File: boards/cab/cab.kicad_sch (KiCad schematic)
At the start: 39 parts, among them J1 Conn_01x08_Female, J2 Conn_01x08_Female, J3 Conn_01x08_Female, J4 Conn_01x08_Female, Q1 SI2308A, Q2 S8550, Q3 BC817-40,215, Q4 S8550, Q5 BC817-40,215, Q6 S8550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

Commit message: Created PCB
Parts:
- added R10: 50k, Resistor_SMD:R_0805_2012Metric, symbol Device:R
- added R11: 4.7k, Resistor_SMD:R_0805_2012Metric, symbol Device:R
- added SW1: SW_Push, Connector_PinHeader_2.54mm:PinHeader_1x02_P2.54mm_Vertical, symbol Switch:SW_Push
- L3: footprint StackCabinet:Solenoid -> TerminalBlock_4Ucon:TerminalBlock_4Ucon_1x02_P3.50mm_Vertical; LCSC. Part# (none) -> C474892; Mfr. Part# (none) -> KF350-3.5-2P
- Q2, Q3, Q4, Q5, Q6, Q7, Q8: footprint Package_TO_SOT_THT:TO-220-3_Vertical -> Package_TO_SOT_SMD:SOT-23
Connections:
- net 5V: now also R10.2
- net GND: now also SW1.1; no longer U1.4 (ON/OFF)
- net CAB_STATE: now reaches U3.10 (PB4)
- net CAB_STATE: now also R10.1, SW1.2
- net RxD: now reaches U3.11 (PB3)
- net TxD: now reaches U3.12 (PB2)
- net 24V_EN: now reaches U3.13 (PB1)
- net 24V_EN: now also U1.4 (ON/OFF)
- net at U3.19 (~{RESET}/PA0): now also R11.1
- new net UPDI: R11.2
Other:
- moved on the sheet: C8, C9

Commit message: Finished schematic
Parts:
- added C10: 0.1uF, Capacitor_SMD:C_0805_2012Metric, symbol Device:C
- added R12: 1k, Resistor_SMD:R_0805_2012Metric, symbol Device:R
- C1, C2: footprint Capacitor_THT:C_Radial_D10.0mm_H16.0mm_P5.00mm -> Capacitor_THT:C_Radial_D12.5mm_H20.0mm_P5.00mm; LCSC Part# C397095 -> (none); LCSC. Part# (none) -> C269945; Mfr. Part# ECR1VGK471MFA100016 -> OGPL41H471MF
- C3, C4, C8, C9: LCSC Part# C91185 -> (none); LCSC. Part# (none) -> C91185
- C5: LCSC Part# C221302 -> (none); LCSC. Part# (none) -> C221302
- C6: LCSC Part# C442870 -> (none); LCSC. Part# (none) -> C442870
- C7: LCSC Part# C152864 -> (none); LCSC. Part# (none) -> C152864
- D1, D2, D3: LCSC Part# C3015221 -> (none); LCSC. Part# (none) -> C3015221
- J1, J2, J3, J4: LCSC. Part# (none) -> C691120; Mfr. Part# (none) -> C691120
- L1: LCSC part# C5142143 -> (none); LCSC. Part# (none) -> C5142143
- L2: footprint Inductor_SMD:L_Wuerth_WE-DD-Typ-L-Typ-XL-Typ-XXL -> Inductor_SMD:L_6.3x6.3_H3; LCSC part# C2846222 -> (none); LCSC. Part# (none) -> C5189964; Mfr. Part# ACPR1208S680MT -> CYA0650-68UH
- Q1: LCSC Part# C347491 -> (none); LCSC. Part# (none) -> C347491
- Q2, Q4, Q6, Q8: LCSC Part# C181159 -> (none); LCSC. Part# (none) -> C181159
- Q3, Q5, Q7: LCSC Part# C52801 -> (none); LCSC. Part# (none) -> C52801
- R1: renamed from R2; LCSC Part# C218493 -> (none); LCSC. Part# (none) -> C218493
- R10: LCSC Part# C2828840 -> (none); LCSC. Part# (none) -> C2828840
- R11: LCSC Part# C115310 -> (none); LCSC. Part# (none) -> C115310
- R2: renamed from R1; LCSC Part# C2828840 -> (none); LCSC. Part# (none) -> C2828840
- R3, R4, R5, R6, R7, R8, R9: LCSC Part# C2902822 -> (none); LCSC. Part# (none) -> C412430; Mfr Part# AR05CTC1000 -> (none); Mfr. Part# (none) -> SWR05JTEV1001
- SW1: LCSC. Part# C393938 -> C397293; Mfr. Part# TS665CJ -> B3F-1005
- U1: footprint Package_SO:SOIC-8_3.9x4.9mm_P1.27mm -> Package_SO:SOP-8_3.9x4.9mm_P1.27mm
- U2: footprint Package_SO:SOIC-8_3.9x4.9mm_P1.27mm -> Package_SO:SOP-8_3.9x4.9mm_P1.27mm; LCSC Part# C61063 -> (none); LCSC. Part# (none) -> C61063
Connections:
- net 24V: now also D2.1 (K); no longer D3.1 (K)
- net 5V: now also C10.1
- net B_PWM: now also R9.1; no longer R5.1
- net GND: now also D3.2 (A), C10.2; no longer D2.2 (A)
- net G_PWM: now also R7.1; no longer R4.1
- net LED1_PWM: now also R5.1; no longer R7.1
- net LED3_PWM: now also R12.1; no longer R9.1
- net R_PWM: now also R4.1; no longer R3.1
- net SOL_EN: now also R3.1; no longer Q1.1 (G)
- net at R7.2: now also Q5.1 (B); no longer Q4.1 (B)
- net at Q8.1 (B): now also R12.2; no longer R9.2
- net at Q7.1 (B): now also R9.2; no longer R5.2
- net at L3.2, Q1.3 (D): now also D2.2 (A); no longer D3.2 (A)
- net at Q3.1 (B): now also R4.2; no longer R3.2
- net at L2.1, U2.2 (OUT): now also D3.1 (K); no longer D2.1 (K)
- new net: Q1.1 (G), R3.2
- new net: Q4.1 (B), R5.2
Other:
- moved on the sheet: SW1

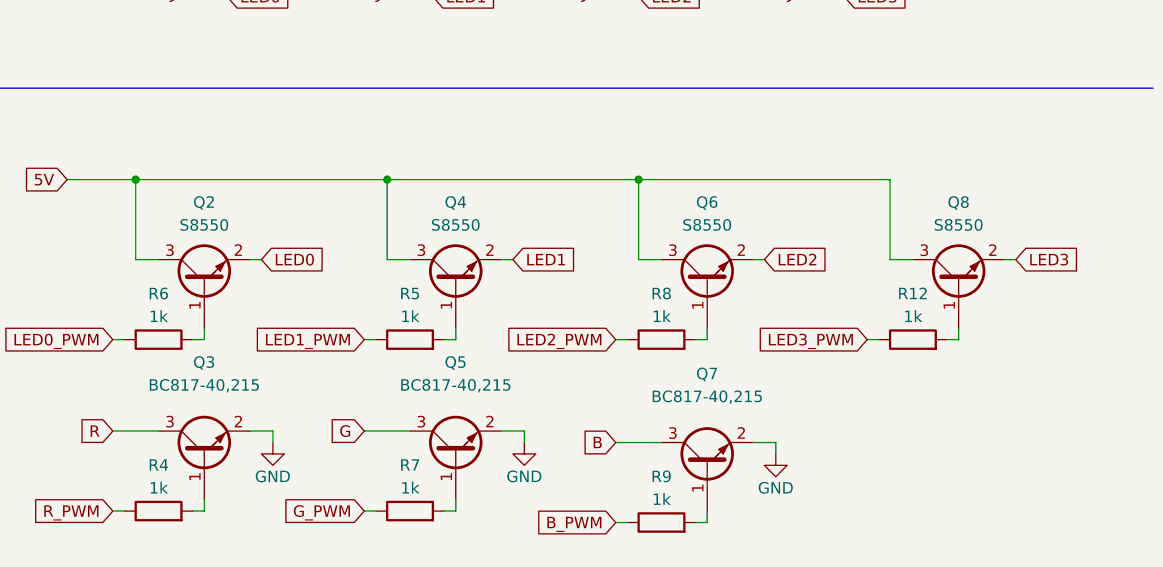
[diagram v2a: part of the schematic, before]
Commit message: Fixed mosfet footprint
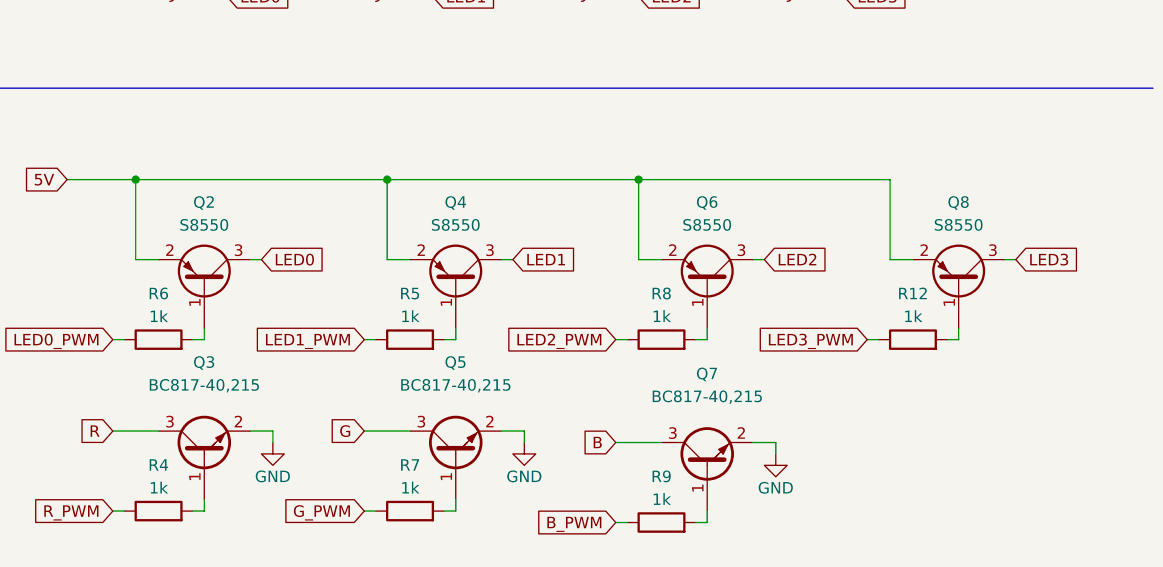
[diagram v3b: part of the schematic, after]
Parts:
- removed Q4, Q6, Q8: S8550, Package_TO_SOT_SMD:SOT-23, symbol Transistor_BJT:2SC1945
- added Q4, Q6, Q8: S8550, Package_TO_SOT_SMD:SOT-23, symbol Transistor_BJT:BC807
- Q2: symbol Transistor_BJT:2SC1945 -> Transistor_BJT:BC807
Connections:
- net 5V: now also Q2.2 (E), Q4.2 (E), Q6.2 (E), Q8.2 (E); no longer Q2.3 (C)
- net LED0: now also Q2.3 (C); no longer Q2.2 (E)
- net LED1: now also Q4.3 (C)
- net LED2: now also Q6.3 (C)
- net LED3: now also Q8.3 (C)
- net at R12.2: now also Q8.1 (B)
- net at R5.2: now also Q4.1 (B)
- net at R8.2: now also Q6.1 (B)
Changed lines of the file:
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@@
     (pin "2")
-  )
-  (symbol (lib_id "Transistor_BJT:2SC1945") (at 262.89 74.93 90) (unit 1)
-    (in_bom yes) (on_board yes)
-    (property "Reference" "Q8" (id 0) (at 262.89 66.04 90))
-    (property "Value" "S8550" (id 1) (at 262.89 68.58 90))
-    (property "Footprint" "Package_TO_SOT_SMD:SOT-23" (id 2) (at 264.795 69.85 0)
-      (effects (font (size 1.27 1.27) italic) (justify left) hide)
-    )
-    (property "Datasheet" "https://datasheet.lcsc.com/lcsc/2205061000_Guangdong-Hottech-S8550_C181159.pdf" (id 3) (at 262.89 74.93 0)
-      (effects (font (size 1.27 1.27)) (justify left) hide)
-    )
-    (property "Mfr. Part#" "S8550" (id 4) (at 262.89 74.93 90)
-      (effects (font (size 1.27 1.27)) hide)
-    )
-    (property "LCSC Part#" "" (id 5) (at 262.89 74.93 90)
-      (effects (font (size 1.27 1.27)) hide)
-    )
-    (property "LCSC. Part#" "C181159" (id 6) (at 262.89 74.93 0)
-      (effects (font (size 1.27 1.27)) hide)
-    )
-    (pin "1")
-    (pin "2")
-    (pin "3")
   )
   (symbol (lib_id "Device:C") (at 123.19 41.91 0) (unit 1)
@@
     (pin "2")
   )
+  (symbol (lib_id "Transistor_BJT:BC807") (at 234.95 74.93 270) (mirror x) (unit 1)
+    (in_bom yes) (on_board yes)
+    (property "Reference" "Q6" (id 0) (at 234.95 66.04 90))
+    (property "Value" "S8550" (id 1) (at 234.95 68.58 90))
+    (property "Footprint" "Package_TO_SOT_SMD:SOT-23" (id 2) (at 233.045 69.85 0)
+      (effects (font (size 1.27 1.27) italic) (justify left) hide)
+    )
+    (property "Datasheet" "https://datasheet.lcsc.com/lcsc/2205061000_Guangdong-Hottech-S8550_C181159.pdf" (id 3) (at 234.95 74.93 0)
+      (effects (font (size 1.27 1.27)) (justify left) hide)
+    )
+    (property "Mfr. Part#" "S8550" (id 4) (at 234.95 74.93 90)
+      (effects (font (size 1.27 1.27)) hide)
+    )
+    (property "LCSC. Part#" "C181159" (id 6) (at 234.95 74.93 0)
+      (effects (font (size 1.27 1.27)) hide)
+    )
+    (pin "1")
+    (pin "2")
+    (pin "3")
+  )
   (symbol (lib_id "power:GND") (at 242.57 93.98 0) (unit 1)
     (in_bom yes) (on_board yes)
@@
     (pin "2")
   )
-  (symbol (lib_id "Transistor_BJT:2SC1945") (at 207.01 74.93 90) (unit 1)
-    (in_bom yes) (on_board yes)
-    (property "Reference" "Q4" (id 0) (at 207.01 66.04 90))
-    (property "Value" "S8550" (id 1) (at 207.01 68.58 90))
-    (property "Footprint" "Package_TO_SOT_SMD:SOT-23" (id 2) (at 208.915 69.85 0)
+  (symbol (lib_id "Transistor_BJT:BC807") (at 262.89 74.93 270) (mirror x) (unit 1)
+    (in_bom yes) (on_board yes)
+    (property "Reference" "Q8" (id 0) (at 262.89 66.04 90))
+    (property "Value" "S8550" (id 1) (at 262.89 68.58 90))
+    (property "Footprint" "Package_TO_SOT_SMD:SOT-23" (id 2) (at 260.985 69.85 0)
       (effects (font (size 1.27 1.27) italic) (justify left) hide)
     )
-    (property "Datasheet" "https://datasheet.lcsc.com/lcsc/2205061000_Guangdong-Hottech-S8550_C181159.pdf" (id 3) (at 207.01 74.93 0)
+    (property "Datasheet" "https://datasheet.lcsc.com/lcsc/2205061000_Guangdong-Hottech-S8550_C181159.pdf" (id 3) (at 262.89 74.93 0)
       (effects (font (size 1.27 1.27)) (justify left) hide)
     )
-    (property "Mfr. Part#" "S8550" (id 4) (at 207.01 74.93 90)
-      (effects (font (size 1.27 1.27)) hide)
-    )
-    (property "LCSC Part#" "" (id 5) (at 207.01 74.93 90)
-      (effects (font (size 1.27 1.27)) hide)
-    )
-    (property "LCSC. Part#" "C181159" (id 6) (at 207.01 74.93 0)
+    (property "Mfr. Part#" "S8550" (id 4) (at 262.89 74.93 90)
+      (effects (font (size 1.27 1.27)) hide)
+    )
+    (property "LCSC. Part#" "C181159" (id 6) (at 262.89 74.93 0)
       (effects (font (size 1.27 1.27)) hide)
     )
@@
     (pin "1")
   )
+  (symbol (lib_id "Transistor_BJT:BC807") (at 207.01 74.93 270) (mirror x) (unit 1)
+    (in_bom yes) (on_board yes)
+    (property "Reference" "Q4" (id 0) (at 207.01 66.04 90))
+    (property "Value" "S8550" (id 1) (at 207.01 68.58 90))
+    (property "Footprint" "Package_TO_SOT_SMD:SOT-23" (id 2) (at 205.105 69.85 0)
+      (effects (font (size 1.27 1.27) italic) (justify left) hide)
+    )
+    (property "Datasheet" "https://datasheet.lcsc.com/lcsc/2205061000_Guangdong-Hottech-S8550_C181159.pdf" (id 3) (at 207.01 74.93 0)
+      (effects (font (size 1.27 1.27)) (justify left) hide)
+    )
+    (property "Mfr. Part#" "S8550" (id 4) (at 207.01 74.93 90)
+      (effects (font (size 1.27 1.27)) hide)
+    )
+    (property "LCSC. Part#" "C181159" (id 6) (at 207.01 74.93 0)
+      (effects (font (size 1.27 1.27)) hide)
+    )
+    (pin "1")
+    (pin "2")
+    (pin "3")
+  )
   (symbol (lib_id "Device:C") (at 44.45 44.45 0) (unit 1)
     (in_bom yes) (on_board yes)
@@
     (pin "5")
   )
-  (symbol (lib_id "Transistor_BJT:2SC1945") (at 179.07 74.93 90) (unit 1)
+  (symbol (lib_id "Transistor_BJT:BC807") (at 179.07 74.93 270) (mirror x) (unit 1)
     (in_bom yes) (on_board yes)
     (property "Reference" "Q2" (id 0) (at 179.07 66.04 90))
     (property "Value" "S8550" (id 1) (at 179.07 68.58 90))
-    (property "Footprint" "Package_TO_SOT_SMD:SOT-23" (id 2) (at 180.975 69.85 0)
+    (property "Footprint" "Package_TO_SOT_SMD:SOT-23" (id 2) (at 177.165 69.85 0)
       (effects (font (size 1.27 1.27) italic) (justify left) hide)
     )
@@
     (pin "1")
   )
-  (symbol (lib_id "Transistor_BJT:2SC1945") (at 234.95 74.93 90) (unit 1)
-    (in_bom yes) (on_board yes)
-    (property "Reference" "Q6" (id 0) (at 234.95 66.04 90))
-    (property "Value" "S8550" (id 1) (at 234.95 68.58 90))
-    (property "Footprint" "Package_TO_SOT_SMD:SOT-23" (id 2) (at 236.855 69.85 0)
-      (effects (font (size 1.27 1.27) italic) (justify left) hide)
-    )
-    (property "Datasheet" "https://datasheet.lcsc.com/lcsc/2205061000_Guangdong-Hottech-S8550_C181159.pdf" (id 3) (at 234.95 74.93 0)
-      (effects (font (size 1.27 1.27)) (justify left) hide)
-    )
-    (property "Mfr. Part#" "S8550" (id 4) (at 234.95 74.93 90)
-      (effects (font (size 1.27 1.27)) hide)
-    )
-    (property "LCSC Part#" "" (id 5) (at 234.95 74.93 90)
-      (effects (font (size 1.27 1.27)) hide)
-    )
-    (property "LCSC. Part#" "C181159" (id 6) (at 234.95 74.93 0)
-      (effects (font (size 1.27 1.27)) hide)
-    )
-    (pin "1")
-    (pin "2")
-    (pin "3")
-  )
   (symbol (lib_id "power:GND") (at 191.77 29.21 0) (unit 1)
     (in_bom yes) (on_board yes)
@@
       (reference "Q3") (unit 1) (value "BC817-40,215") (footprint "Package_TO_SOT_SMD:SOT-23")
     )
-    (path "/59ddffe5-0dff-4bee-a16e-bf5bc8ab3f34"
+    (path "/773b2310-3334-4f95-9a81-1e66c9eb0eb2"
       (reference "Q4") (unit 1) (value "S8550") (footprint "Package_TO_SOT_SMD:SOT-23")
     )
@@
       (reference "Q5") (unit 1) (value "BC817-40,215") (footprint "Package_TO_SOT_SMD:SOT-23")
     )
-    (path "/fbeaaf82-15a7-47c8-9550-6b0c20c4284d"
+    (path "/21e6e123-f380-4d1f-aea4-53d262ccd85a"
       (reference "Q6") (unit 1) (value "S8550") (footprint "Package_TO_SOT_SMD:SOT-23")
     )
@@
       (reference "Q7") (unit 1) (value "BC817-40,215") (footprint "Package_TO_SOT_SMD:SOT-23")
     )
-    (path "/03c9e3a6-520e-43cf-ac75-75db95716ba5"
+    (path "/5d515d29-5c44-4bed-9ff1-10a60546f72b"
       (reference "Q8") (unit 1) (value "S8550") (footprint "Package_TO_SOT_SMD:SOT-23")
     )

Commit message: Placed Power, Attiny and LED power
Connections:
- net TxD is gone; now on net GDA: U3.12 (PB2)
- net 24V: now also C5.1, C7.1, L1.2, R2.2; no longer C6.1, L2.2, U2.3 (FB)
- net 24V_EN: now also U3.2 (PA3); no longer U3.13 (PB1)
- net 5V: now also C6.1, L2.2, U2.3 (FB); no longer C5.1, C7.1, L1.2, R2.2
- net G_PWM: now also U3.7 (PA6); no longer U3.2 (PA3)
- net LED1_PWM: now also U3.14 (PB0); no longer U3.6 (PA5)
- net LED2_PWM: now also U3.13 (PB1); no longer U3.7 (PA6)
- net R_PWM: now also U3.6 (PA5); no longer U3.1 (PA2)
- net SOL_EN: now also U3.1 (PA2); no longer U3.14 (PB0)
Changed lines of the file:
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@@
+    )
+  )
+  (global_label "R_PWM" (shape input) (at 137.16 143.51 0) (fields_autoplaced)
+    (effects (font (size 1.27 1.27)) (justify left))
+    (property "Intersheet References" "${INTERSHEET_REFS}" (id 0) (at 145.9836 143.5894 0)
+      (effects (font (size 1.27 1.27)) (justify left) hide)
     )
   )
@@
     )
   )
+  (global_label "LED1_PWM" (shape input) (at 137.16 153.67 0) (fields_autoplaced)
+    (effects (font (size 1.27 1.27)) (justify left))
+    (property "Intersheet References" "${INTERSHEET_REFS}" (id 0) (at 149.3702 153.7494 0)
+      (effects (font (size 1.27 1.27)) (justify left) hide)
+    )
+  )
   (global_label "LED3_PWM" (shape input) (at 252.73 81.28 180) (fields_autoplaced)
     (effects (font (size 1.27 1.27)) (justify right))
@@
     )
   )
-  (global_label "24V_EN" (shape input) (at 137.16 156.21 0) (fields_autoplaced)
-    (effects (font (size 1.27 1.27)) (justify left))
-    (property "Intersheet References" "${INTERSHEET_REFS}" (id 0) (at 146.5279 156.1306 0)
-      (effects (font (size 1.27 1.27)) (justify left) hide)
-    )
-  )
   (global_label "SOL_EN" (shape input) (at 45.72 158.75 180) (fields_autoplaced)
     (effects (font (size 1.27 1.27)) (justify right))
@@
     )
   )
-  (global_label "24V" (shape input) (at 115.57 81.28 0) (fields_autoplaced)
-    (effects (font (size 1.27 1.27)) (justify left))
-    (property "Intersheet References" "${INTERSHEET_REFS}" (id 0) (at 121.4907 81.2006 0)
+  (global_label "5V" (shape input) (at 115.57 81.28 0) (fields_autoplaced)
+    (effects (font (size 1.27 1.27)) (justify left))
+    (property "Intersheet References" "${INTERSHEET_REFS}" (id 0) (at 120.2812 81.2006 0)
       (effects (font (size 1.27 1.27)) (justify left) hide)
     )
@@
     )
   )
-  (global_label "LED2_PWM" (shape input) (at 137.16 146.05 0) (fields_autoplaced)
-    (effects (font (size 1.27 1.27)) (justify left))
-    (property "Intersheet References" "${INTERSHEET_REFS}" (id 0) (at 149.3702 146.1294 0)
-      (effects (font (size 1.27 1.27)) (justify left) hide)
-    )
-  )
   (global_label "24V_EN" (shape input) (at 50.8 39.37 0) (fields_autoplaced)
     (effects (font (size 1.27 1.27)) (justify left))
@@
     )
   )
-  (global_label "G_PWM" (shape input) (at 137.16 138.43 0) (fields_autoplaced)
-    (effects (font (size 1.27 1.27)) (justify left))
-    (property "Intersheet References" "${INTERSHEET_REFS}" (id 0) (at 145.9836 138.5094 0)
+  (global_label "24V_EN" (shape input) (at 137.16 138.43 0) (fields_autoplaced)
+    (effects (font (size 1.27 1.27)) (justify left))
+    (property "Intersheet References" "${INTERSHEET_REFS}" (id 0) (at 146.5279 138.3506 0)
       (effects (font (size 1.27 1.27)) (justify left) hide)
     )
@@
     )
   )
-  (global_label "R_PWM" (shape input) (at 137.16 135.89 0) (fields_autoplaced)
-    (effects (font (size 1.27 1.27)) (justify left))
-    (property "Intersheet References" "${INTERSHEET_REFS}" (id 0) (at 145.9836 135.9694 0)
+  (global_label "SOL_EN" (shape input) (at 137.16 135.89 0) (fields_autoplaced)
+    (effects (font (size 1.27 1.27)) (justify left))
+    (property "Intersheet References" "${INTERSHEET_REFS}" (id 0) (at 146.5883 135.8106 0)
       (effects (font (size 1.27 1.27)) (justify left) hide)
     )
@@
     )
   )
-  (global_label "TxD" (shape input) (at 137.16 158.75 0) (fields_autoplaced)
-    (effects (font (size 1.27 1.27)) (justify left))
-    (property "Intersheet References" "${INTERSHEET_REFS}" (id 0) (at 142.8388 158.6706 0)
+  (global_label "GDA" (shape input) (at 137.16 158.75 0) (fields_autoplaced)
+    (effects (font (size 1.27 1.27)) (justify left))
+    (property "Intersheet References" "${INTERSHEET_REFS}" (id 0) (at 143.2017 158.6706 0)
       (effects (font (size 1.27 1.27)) (justify left) hide)
     )
@@
     )
   )
+  (global_label "G_PWM" (shape input) (at 137.16 146.05 0) (fields_autoplaced)
+    (effects (font (size 1.27 1.27)) (justify left))
+    (property "Intersheet References" "${INTERSHEET_REFS}" (id 0) (at 145.9836 145.9706 0)
+      (effects (font (size 1.27 1.27)) (justify left) hide)
+    )
+  )
   (global_label "G" (shape input) (at 196.85 91.44 180) (fields_autoplaced)
     (effects (font (size 1.27 1.27)) (justify right))
@@
     )
   )
-  (global_label "SOL_EN" (shape input) (at 137.16 153.67 0) (fields_autoplaced)
-    (effects (font (size 1.27 1.27)) (justify left))
-    (property "Intersheet References" "${INTERSHEET_REFS}" (id 0) (at 146.5883 153.5906 0)
-      (effects (font (size 1.27 1.27)) (justify left) hide)
-    )
-  )
   (global_label "GDA" (shape input) (at 250.19 33.02 0) (fields_autoplaced)
     (effects (font (size 1.27 1.27)) (justify left))
@@
     )
   )
-  (global_label "5V" (shape input) (at 132.08 34.29 0) (fields_autoplaced)
-    (effects (font (size 1.27 1.27)) (justify left))
-    (property "Intersheet References" "${INTERSHEET_REFS}" (id 0) (at 136.7912 34.2106 0)
+  (global_label "24V" (shape input) (at 132.08 34.29 0) (fields_autoplaced)
+    (effects (font (size 1.27 1.27)) (justify left))
+    (property "Intersheet References" "${INTERSHEET_REFS}" (id 0) (at 138.0007 34.2106 0)
       (effects (font (size 1.27 1.27)) (justify left) hide)
     )
@@
     )
   )
-  (global_label "LED1_PWM" (shape input) (at 137.16 143.51 0) (fields_autoplaced)
-    (effects (font (size 1.27 1.27)) (justify left))
-    (property "Intersheet References" "${INTERSHEET_REFS}" (id 0) (at 149.3702 143.5894 0)
-      (effects (font (size 1.27 1.27)) (justify left) hide)
-    )
-  )
   (global_label "B" (shape input) (at 204.47 38.1 0) (fields_autoplaced)
     (effects (font (size 1.27 1.27)) (justify left))
@@
     (property "Intersheet References" "${INTERSHEET_REFS}" (id 0) (at 221.1069 92.6306 0)
       (effects (font (size 1.27 1.27)) (justify right) hide)
+    )
+  )
+  (global_label "LED2_PWM" (shape input) (at 137.16 156.21 0) (fields_autoplaced)
+    (effects (font (size 1.27 1.27)) (justify left))
+    (property "Intersheet References" "${INTERSHEET_REFS}" (id 0) (at 149.3702 156.2894 0)
+      (effects (font (size 1.27 1.27)) (justify left) hide)
     )
   )
@@
       (effects (font (size 1.27 1.27)) hide)
     )
-    (property "LCSC Part#" "" (id 5) (at 55.88 152.4 0)
-      (effects (font (size 1.27 1.27)) hide)
-    )

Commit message: Routing & planes
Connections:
- net 24V_EN: now also U3.1 (PA2); no longer U3.2 (PA3)
- net B_PWM: now also U3.9 (PB5); no longer U3.5 (PA4)
- net CAB_STATE: now also U3.5 (PA4); no longer U3.10 (PB4)
- net G_PWM: now also U3.13 (PB1); no longer U3.7 (PA6)
- net LED0_PWM: now also U3.8 (PA7); no longer U3.20 (PA1)
- net LED2_PWM: now also U3.10 (PB4); no longer U3.13 (PB1)
- net LED3_PWM: now also U3.6 (PA5); no longer U3.8 (PA7)
- net R_PWM: now also U3.7 (PA6); no longer U3.6 (PA5)
- net SOL_EN: now also U3.20 (PA1); no longer U3.1 (PA2)
- net SOL_R: now reaches D2.2 (A), L3.2, Q1.3 (D)
